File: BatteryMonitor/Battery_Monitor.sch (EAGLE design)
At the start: 40 parts, among them IC1 MAX232

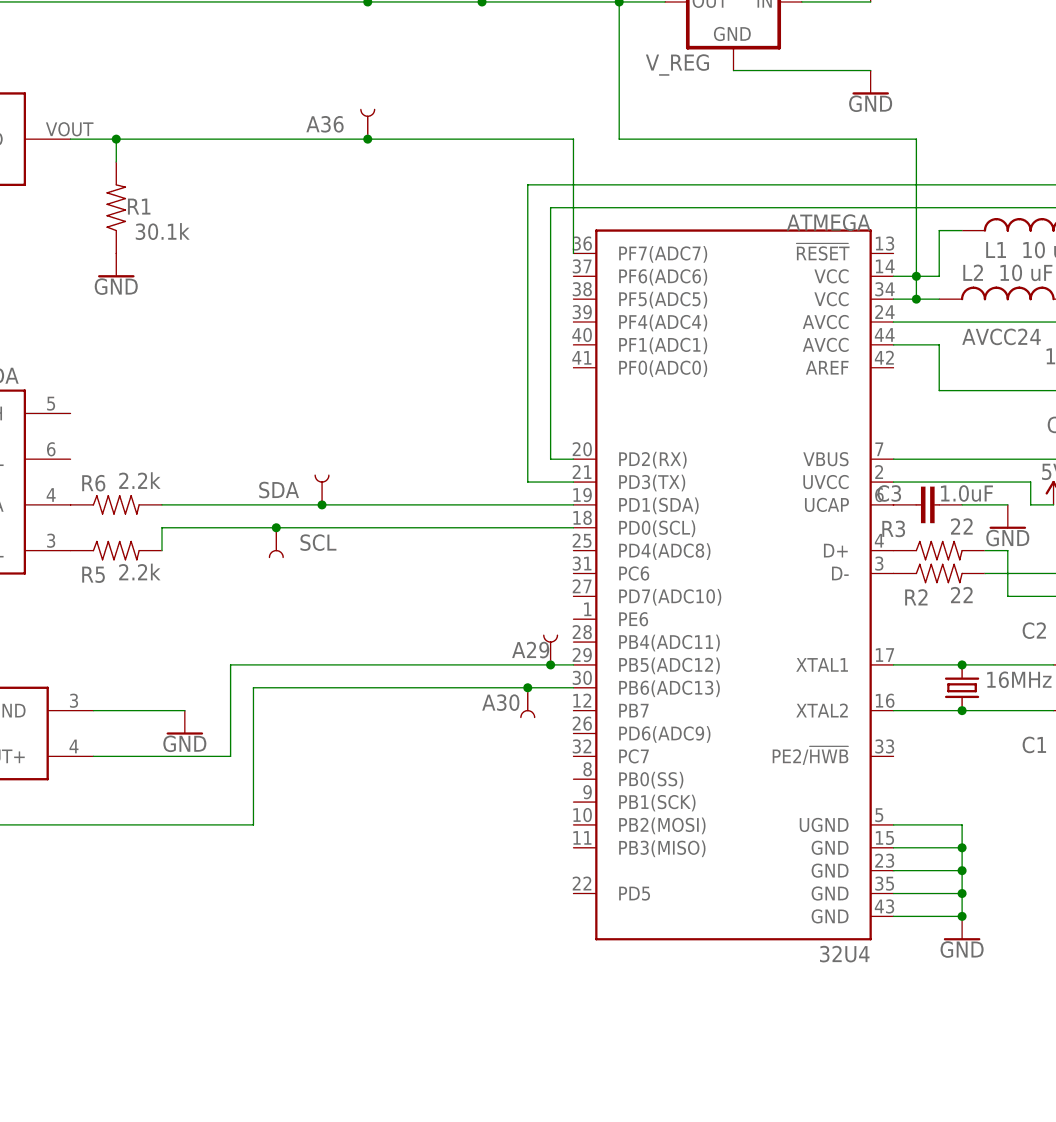
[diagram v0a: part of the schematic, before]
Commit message: Battery monitor board is updated with spi headers
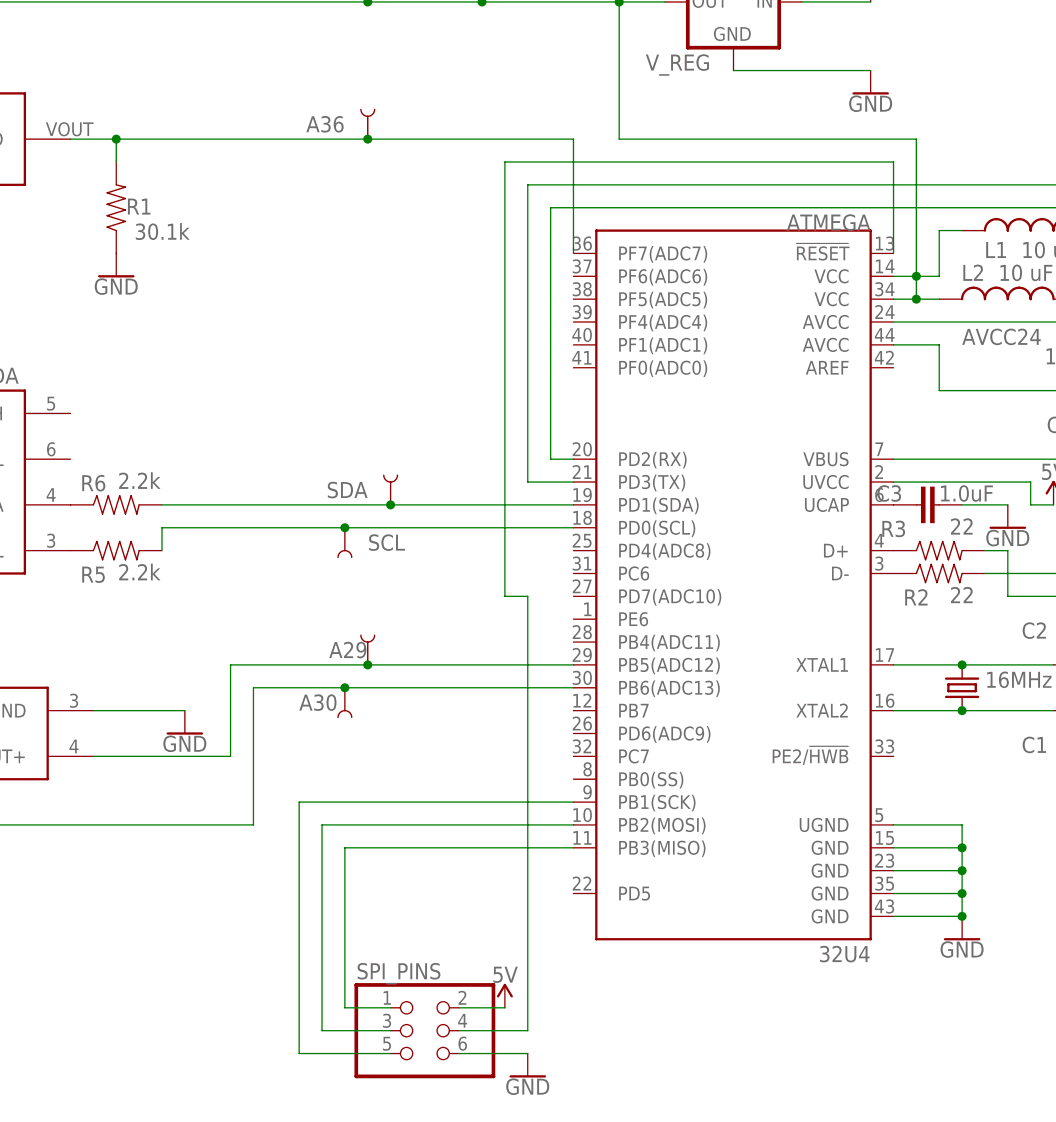
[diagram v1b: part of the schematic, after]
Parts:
- added SPI_PINS: (no value), pinhead:PINHD-2X3
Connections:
- new net MISO: ATMEGA.PB3(MISO), SPI_PINS.1
- new net MOSI: ATMEGA.PB2(MOSI), SPI_PINS.3
- new net RESET: ATMEGA.!RESET, SPI_PINS.4
- new net SCK: ATMEGA.PB1(SCK), SPI_PINS.5
- net 5V: now also SPI_PINS.2
- net GND: now also SPI_PINS.6
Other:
- moved on the sheet: A29, A30, SCL, SDA
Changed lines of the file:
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@@
 <part name="C14" library="SparkFun-Capacitors" deviceset="10UF" device="-0603-6.3V-20%" value="10uF"/>
 <part name="GND16" library="SparkFun-PowerSymbols" deviceset="GND" device=""/>
+<part name="SUPPLY6" library="SparkFun-PowerSymbols" deviceset="5V" device=""/>
+<part name="GND17" library="SparkFun-PowerSymbols" deviceset="GND" device=""/>
+<part name="SPI_PINS" library="pinhead" library_urn="urn:adsk.eagle:library:325" deviceset="PINHD-2X3" device="" package3d_urn="urn:adsk.eagle:package:22462/2"/>
 </parts>
 <sheets>
@@
 <attribute name="NAME" x="228.6" y="175.26" size="1.778" layer="95" font="vector" rot="R180"/>
 </instance>
-<instance part="SDA" gate="G$1" x="76.2" y="93.98" smashed="yes" rot="R90">
-<attribute name="NAME" x="73.66" y="96.52" size="1.778" layer="95" font="vector" rot="R180"/>
-</instance>
-<instance part="SCL" gate="G$1" x="71.12" y="91.44" smashed="yes" rot="R270">
-<attribute name="NAME" x="73.66" y="88.9" size="1.778" layer="95" font="vector"/>
-</instance>
-<instance part="A29" gate="G$1" x="101.6" y="76.2" smashed="yes" rot="R90">
-<attribute name="NAME" x="101.6" y="78.74" size="1.778" layer="95" font="vector" rot="R180"/>
-</instance>
-<instance part="A30" gate="G$1" x="99.06" y="73.66" smashed="yes" rot="R270">
-<attribute name="NAME" x="93.98" y="71.12" size="1.778" layer="95" font="vector"/>
+<instance part="SDA" gate="G$1" x="83.82" y="93.98" smashed="yes" rot="R90">
+<attribute name="NAME" x="81.28" y="96.52" size="1.778" layer="95" font="vector" rot="R180"/>
+</instance>
+<instance part="SCL" gate="G$1" x="78.74" y="91.44" smashed="yes" rot="R270">
+<attribute name="NAME" x="81.28" y="88.9" size="1.778" layer="95" font="vector"/>
+</instance>
+<instance part="A29" gate="G$1" x="81.28" y="76.2" smashed="yes" rot="R90">
+<attribute name="NAME" x="81.28" y="78.74" size="1.778" layer="95" font="vector" rot="R180"/>
+</instance>
+<instance part="A30" gate="G$1" x="78.74" y="73.66" smashed="yes" rot="R270">
+<attribute name="NAME" x="73.66" y="71.12" size="1.778" layer="95" font="vector"/>
 </instance>
 <instance part="MEGA_TX" gate="G$1" x="180.34" y="129.54" smashed="yes" rot="R90">
@@
 </instance>
 <instance part="GND16" gate="1" x="180.34" y="96.52"/>
+<instance part="SUPPLY6" gate="G$1" x="96.52" y="38.1"/>
+<instance part="GND17" gate="1" x="99.06" y="30.48"/>
+<instance part="SPI_PINS" gate="A" x="86.36" y="35.56"/>
 </instances>
 <busses>
@@
 <pinref part="GND16" gate="1" pin="GND"/>
 <wire x1="180.34" y1="99.06" x2="167.64" y2="99.06" width="0.1524" layer="91"/>
+</segment>
+<segment>
+<pinref part="GND17" gate="1" pin="GND"/>
+<pinref part="SPI_PINS" gate="A" pin="6"/>
+<wire x1="99.06" y1="33.02" x2="91.44" y2="33.02" width="0.1524" layer="91"/>
 </segment>
 </net>
@@
 <junction x="93.98" y="149.86"/>
 </segment>
+<segment>
+<pinref part="SUPPLY6" gate="G$1" pin="5V"/>
+<pinref part="SPI_PINS" gate="A" pin="2"/>
+<wire x1="96.52" y1="38.1" x2="91.44" y2="38.1" width="0.1524" layer="91"/>
+</segment>
 </net>
 <net name="A36" class="0">
@@
 <pinref part="ATMEGA" gate="G$1" pin="PD1(SDA)"/>
 <pinref part="R6" gate="G$1" pin="2"/>
-<wire x1="104.14" y1="93.98" x2="76.2" y2="93.98" width="0.1524" layer="91"/>
+<wire x1="104.14" y1="93.98" x2="83.82" y2="93.98" width="0.1524" layer="91"/>
 <pinref part="SDA" gate="G$1" pin="1"/>
-<wire x1="76.2" y1="93.98" x2="58.42" y2="93.98" width="0.1524" layer="91"/>
-<junction x="76.2" y="93.98"/>
+<wire x1="83.82" y1="93.98" x2="58.42" y2="93.98" width="0.1524" layer="91"/>
+<junction x="83.82" y="93.98"/>
 </segment>
 </net>
@@
 <segment>
 <pinref part="ATMEGA" gate="G$1" pin="PD0(SCL)"/>
-<wire x1="104.14" y1="91.44" x2="71.12" y2="91.44" width="0.1524" layer="91"/>
+<wire x1="104.14" y1="91.44" x2="78.74" y2="91.44" width="0.1524" layer="91"/>
 <pinref part="R5" gate="G$1" pin="2"/>
-<wire x1="71.12" y1="91.44" x2="58.42" y2="91.44" width="0.1524" layer="91"/>
+<wire x1="78.74" y1="91.44" x2="58.42" y2="91.44" width="0.1524" layer="91"/>
 <wire x1="58.42" y1="91.44" x2="58.42" y2="88.9" width="0.1524" layer="91"/>
 <pinref part="SCL" gate="G$1" pin="1"/>
-<junction x="71.12" y="91.44"/>
+<junction x="78.74" y="91.44"/>
 </segment>
 </net>
 <net name="A29" class="0">
 <segment>
-<wire x1="101.6" y1="76.2" x2="66.04" y2="76.2" width="0.1524" layer="91"/>
+<wire x1="81.28" y1="76.2" x2="66.04" y2="76.2" width="0.1524" layer="91"/>
 <wire x1="66.04" y1="76.2" x2="66.04" y2="66.04" width="0.1524" layer="91"/>
 <pinref part="PRESSURE" gate="G$1" pin="VOUT+"/>
 <wire x1="66.04" y1="66.04" x2="50.8" y2="66.04" width="0.1524" layer="91"/>
 <pinref part="ATMEGA" gate="G$1" pin="PB5(ADC12)"/>
-<wire x1="104.14" y1="76.2" x2="101.6" y2="76.2" width="0.1524" layer="91"/>
+<wire x1="104.14" y1="76.2" x2="81.28" y2="76.2" width="0.1524" layer="91"/>
 <pinref part="A29" gate="G$1" pin="1"/>
-<junction x="101.6" y="76.2"/>
+<junction x="81.28" y="76.2"/>
 </segment>
 </net>
@@
 <wire x1="20.32" y1="58.42" x2="20.32" y2="66.04" width="0.1524" layer="91"/>
 <pinref part="ATMEGA" gate="G$1" pin="PB6(ADC13)"/>
-<wire x1="104.14" y1="73.66" x2="99.06" y2="73.66" width="0.1524" layer="91"/>
-<wire x1="68.58" y1="73.66" x2="99.06" y2="73.66" width="0.1524" layer="91"/>
+<wire x1="104.14" y1="73.66" x2="78.74" y2="73.66" width="0.1524" layer="91"/>
+<wire x1="68.58" y1="73.66" x2="78.74" y2="73.66" width="0.1524" layer="91"/>
 <pinref part="A30" gate="G$1" pin="1"/>
-<junction x="99.06" y="73.66"/>
+<junction x="78.74" y="73.66"/>
 </segment>
 </net>
@@
 </segment>
 </net>
+<net name="MISO" class="0">
+<segment>
+<pinref part="ATMEGA" gate="G$1" pin="PB3(MISO)"/>
+<wire x1="104.14" y1="55.88" x2="78.74" y2="55.88" width="0.1524" layer="91"/>
+<wire x1="78.74" y1="55.88" x2="78.74" y2="38.1" width="0.1524" layer="91"/>
+<pinref part="SPI_PINS" gate="A" pin="1"/>
+<wire x1="78.74" y1="38.1" x2="83.82" y2="38.1" width="0.1524" layer="91"/>
+</segment>
+</net>
+<net name="MOSI" class="0">
+<segment>
+<wire x1="76.2" y1="35.56" x2="76.2" y2="58.42" width="0.1524" layer="91"/>
+<pinref part="ATMEGA" gate="G$1" pin="PB2(MOSI)"/>
+<wire x1="76.2" y1="58.42" x2="104.14" y2="58.42" width="0.1524" layer="91"/>
+<pinref part="SPI_PINS" gate="A" pin="3"/>
+<wire x1="76.2" y1="35.56" x2="83.82" y2="35.56" width="0.1524" layer="91"/>
+</segment>
+</net>
+<net name="RESET" class="0">
+<segment>
+<pinref part="ATMEGA" gate="G$1" pin="!RESET"/>
+<wire x1="139.7" y1="121.92" x2="139.7" y2="132.08" width="0.1524" layer="91"/>
+<wire x1="139.7" y1="132.08" x2="96.52" y2="132.08" width="0.1524" layer="91"/>
+<wire x1="99.06" y1="35.56" x2="99.06" y2="83.82" width="0.1524" layer="91"/>
+<wire x1="99.06" y1="83.82" x2="96.52" y2="83.82" width="0.1524" layer="91"/>
+<wire x1="96.52" y1="83.82" x2="96.52" y2="132.08" width="0.1524" layer="91"/>
+<pinref part="SPI_PINS" gate="A" pin="4"/>
+<wire x1="99.06" y1="35.56" x2="91.44" y2="35.56" width="0.1524" layer="91"/>
+</segment>
+</net>
+<net name="SCK" class="0">
+<segment>
+<pinref part="ATMEGA" gate="G$1" pin="PB1(SCK)"/>
+<wire x1="104.14" y1="60.96" x2="73.66" y2="60.96" width="0.1524" layer="91"/>
+<wire x1="73.66" y1="60.96" x2="73.66" y2="33.02" width="0.1524" layer="91"/>
+<pinref part="SPI_PINS" gate="A" pin="5"/>
+<wire x1="73.66" y1="33.02" x2="83.82" y2="33.02" width="0.1524" layer="91"/>
+</segment>
+</net>
